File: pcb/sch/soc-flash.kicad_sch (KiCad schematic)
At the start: 4 parts, among them U3 S25FL128SAGNFV003

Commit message: more pin definition pending define for how boot mode and power cycling will work, potential uc (stm32)
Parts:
- added C901: 0.1uF, Capacitor_SMD:C_0402_1005Metric, symbol library:C
- R901: renamed from R6; value 4.7K -> 10K; Manufacturer YAGEO -> (none); Manufacturer Product Number RC0402FR-074K7L -> (none); now not fitted
- R902: renamed from R7; value 4.7K -> 10K; Manufacturer YAGEO -> (none); Manufacturer Product Number RC0402FR-074K7L -> (none); now not fitted
- R903: renamed from R8; value 4.7K -> 10K; Manufacturer YAGEO -> (none); Manufacturer Product Number RC0402FR-074K7L -> (none); now not fitted
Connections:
- net 3V3_FD: now also C901.2
- net GND: now also C901.1

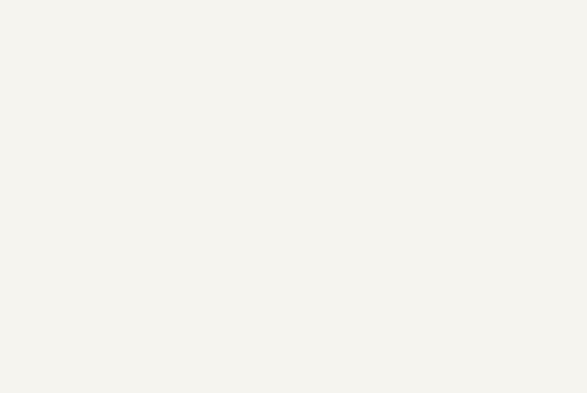
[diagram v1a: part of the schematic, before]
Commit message: fices for boot definition
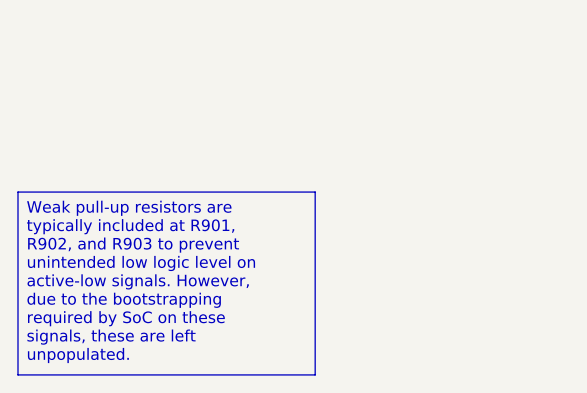
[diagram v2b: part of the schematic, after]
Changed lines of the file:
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@@
 		(rev "2.0")
+	)
+	(text_box "Weak pull-up resistors are typically included at R901, R902, and R903 to prevent unintended low logic level on active-low signals. However, due to the bootstrapping required by SoC on these signals, these are left unpopulated."
+		(exclude_from_sim no)
+		(at 15.24 175.26 0)
+		(size 33.02 20.32)
+		(margins 0.9525 0.9525 0.9525 0.9525)
+		(stroke
+			(width 0)
+			(type solid)
+			(color 0 0 0 1)
+		)
+		(fill
+			(type color)
+			(color 255 229 191 1)
+		)
+		(effects
+			(font
+				(size 1.27 1.27)
+				(color 0 0 0 1)
+			)
+			(justify left top)
+		)
 	)
 	(junction

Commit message: power
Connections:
- net 3V3_FD renamed 3V3_Z
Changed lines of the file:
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@@
 		)
 	)
-	(hierarchical_label "3V3_FD"
+	(hierarchical_label "3V3_Z"
 		(shape input)
 		(at 121.92 83.82 180)
@@
 		)
 	)
-	(hierarchical_label "3V3_FD"
+	(hierarchical_label "3V3_Z"
 		(shape input)
 		(at 139.7 109.22 180)
